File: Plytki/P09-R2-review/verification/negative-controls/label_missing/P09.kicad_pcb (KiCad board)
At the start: 2 copper layers, 53 x 100 mm, 50 parts, among them J1 J_BP, J2 SERWIS, J3 TC1, J4 TC2, U1 74LVC125AD, U2 74LVC125AD, U3 SN74HC139N

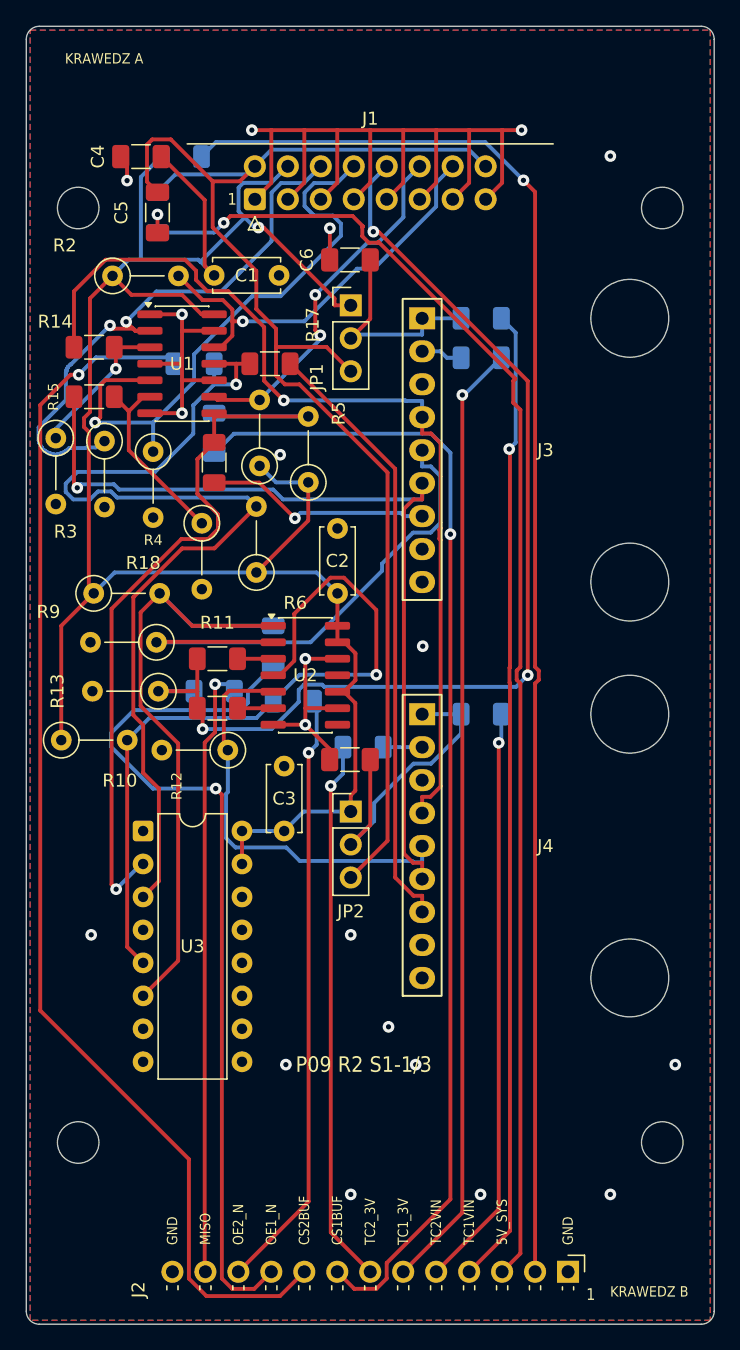
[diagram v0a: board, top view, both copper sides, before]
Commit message: P09 R2 PCB: moduły lutowane wprost i poprawki po recenzji
- J3/J4: MAX31856 XU lutowane wprost fabryczną listwą (decyzja użytkownika 1.10):
  footprint MAX31856_XU bez otworów podparcia; wysokość szacunek górny 14,1 mm
- rozmieszczenie: JP1 pod J3.1 jak JP2 (C6/C7 4,0/4,25 mm, próg 6 mm), pas krawędzi A wolny
- nadruk: tytuł ze slotem, znaki pinu 1 przy J3/J4, pełne nazwy kołków, oznaczenia
  bliżej swojej części i poza strefami Ø7, ukryte oznaczenia z F.Fab na montażu
- kontrole PCB 25/25 (etykiety z tabeli LABEL, pas A, znaki pinu 1, bliskość, tytuł),
  próby ujemne 22/22; gnd_pour_removed usuwa wylewkę w pliku (b.Remove() psuł SWIG)
- nowe trasowanie: 56 przelotek, bez tras planera; PDF obejrzany (5 stron)
- dokumenty: PROJEKT, ODBIOR, MODUL-KWALIFIKACJA, ZAKUPY, README

Co-Authored-By: Claude Opus 5.5 <noreply@anthropic.com>
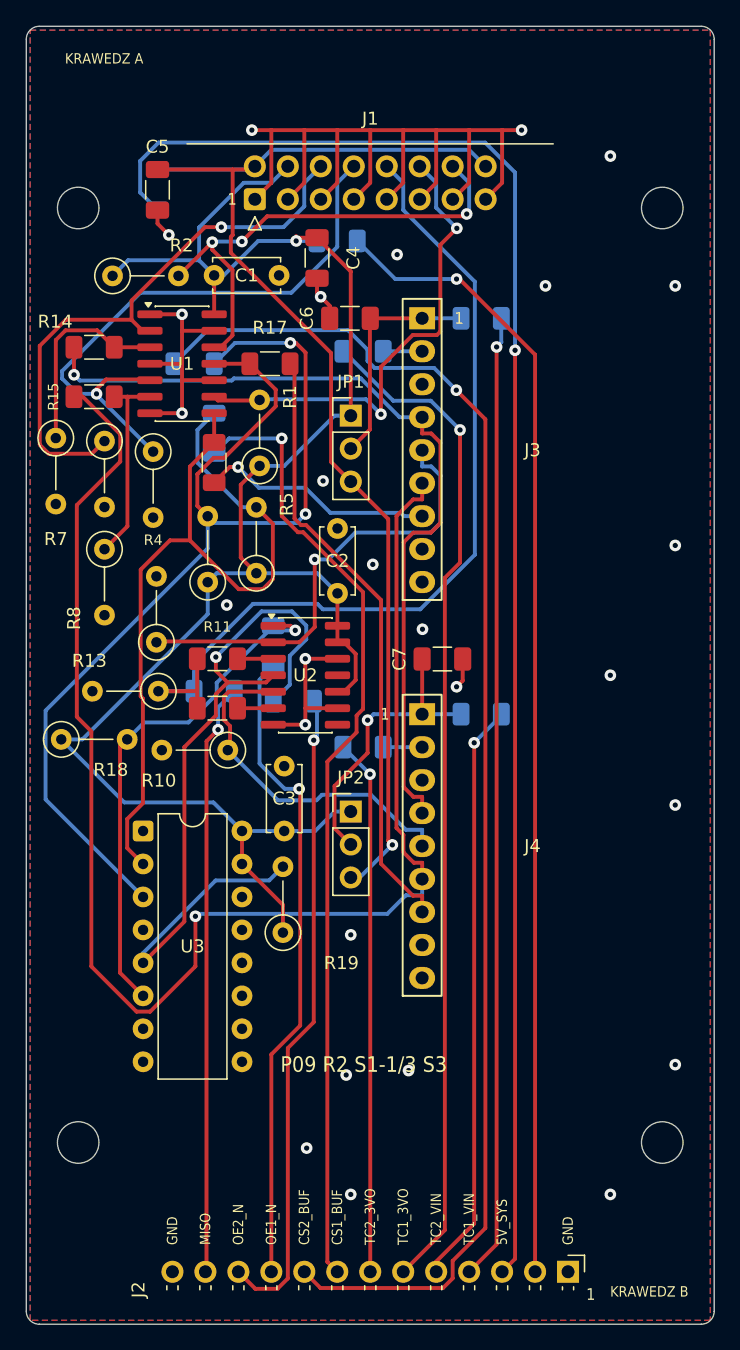
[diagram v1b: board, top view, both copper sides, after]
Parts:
- J3, J4: footprint P09:MAX31856_XU_socket -> P09:MAX31856_XU
- moved R19 22.6 mm to (19.8, 69.8), turned to 90 degrees
- moved C4 15.7 mm to (22.4, 17.9), turned to -90 degrees
- moved R20 13.6 mm to (23.9, 16.5)
- moved R18 11.5 mm to (2.69, 54.9)
- moved C7 10.5 mm to (32.1, 48.8), turned to 0 degrees
- moved R24 9.11 mm to (25.9, 25.0), turned to 180 degrees
- moved JP1 8.50 mm to (25.0, 30.0)
- moved R5 8.06 mm to (17.7, 42.1)
- moved R8 7.76 mm to (6.03, 40.3)
- moved C6 4.50 mm to (24.9, 22.5)
- moved R6 3.82 mm to (14.0, 42.8)
- moved C5 1.75 mm to (10.1, 12.6)
- moved R21 1.75 mm to (10.1, 12.6)
- turned R9 to 90 degrees
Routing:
- net MOSI_MODULE: track 68.0 -> 114.7 mm
- net /CONNECT/SRV_3V3_IO: track 111.2 -> 88.0 mm
- net 3V3_IO: track 162.0 -> 139.9 mm
- net /CONNECT/SRV_OE1_N: track 68.2 -> 50.0 mm
- net /CONNECT/SRV_5V_SYS: track 103.8 -> 119.9 mm
- net /CONNECT/SRV_CS1_BUF: track 89.8 -> 74.2 mm
- net SPI3_MISO: track 83.8 -> 69.9 mm, vias 3 -> 0
- net /CONNECT/SRV_CS2_BUF: track 94.3 -> 107.9 mm
- net 5V_SYS: track 109.0 -> 95.5 mm, vias 0 -> 1
- net OE1_N: track 53.5 -> 40.2 mm, vias 0 -> 1
- net TC1_CS: track 27.5 -> 37.3 mm
- net CLK_MODULE: track 73.3 -> 64.9 mm
- net CS2_BUF: track 76.6 -> 84.5 mm, vias 1 -> 2
- net TC1_MISO: track 41.6 -> 35.4 mm, vias 0 -> 1
- net TC2_CS: track 32.0 -> 38.1 mm, vias 1 -> 3
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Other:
- board text added: "CS1_BUF"
- board text added: "CS2_BUF"
- board text added: "P09 R2 S1-1/3 S3"
- board text added: "TC1_3VO"
- board text added: "TC1_VIN"
- board text added: "TC2_3VO"
- board text added: "TC2_VIN"
- board text removed: "CS1BUF"
- board text removed: "CS2BUF"
- board text removed: "P09 R2 S1-1/3"
- board text removed: "TC1VIN"
- board text removed: "TC1_3V"
- board text removed: "TC2VIN"
- board text removed: "TC2_3V"
